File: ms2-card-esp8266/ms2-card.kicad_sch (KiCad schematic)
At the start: 63 parts, among them J1 Schaltregler, J10 MicroSD_SPI_CD, J11 Conn_01x06, J2 ESP Prog, J20 Smartcard Connector, J21 PogoPin, J22 Card Edge, J23 Conn_01x04, J30 USB_B_Micro, J31 Power Select, J32 Conn_01x03, Q1 MMBT3904, Q2 MMBT3904, Q3 MMBT5401, SW1 RESET, U1 ESP-12F, U10 W25Q128JVIM, U2 FM24C64B, U20 BL1551B, U3 BL1551B, U30 CP2102N-A02-GQFN24R, U4 BL1551B, U6 AMS1117-3.3

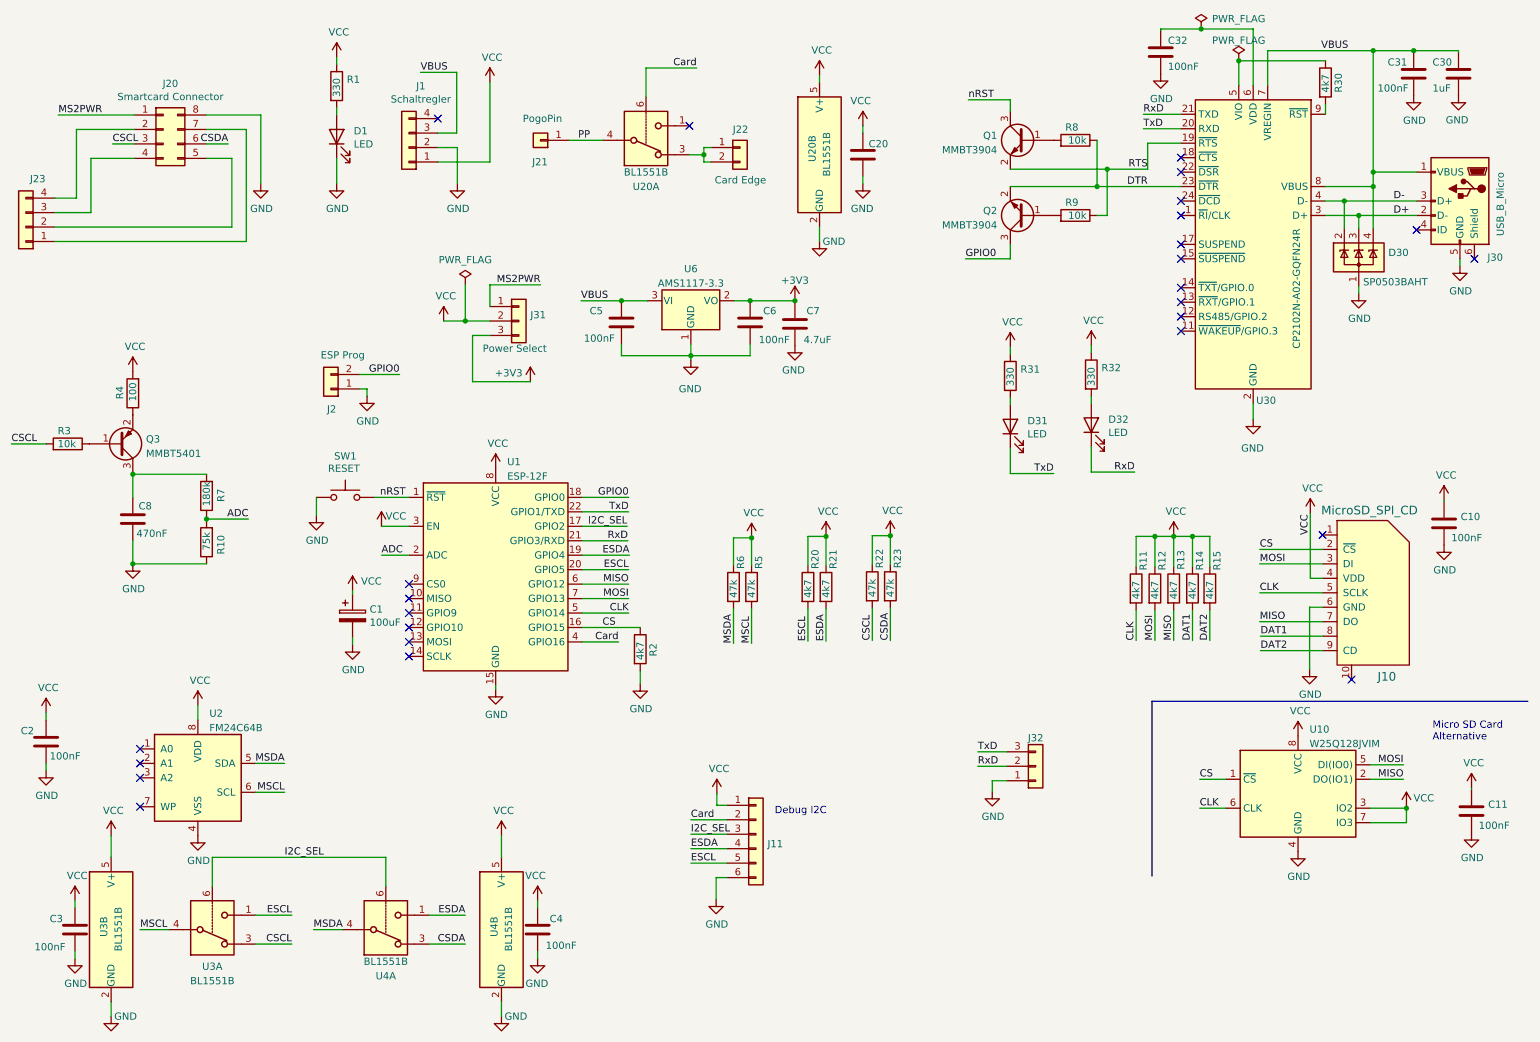
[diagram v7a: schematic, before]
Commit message: switch to KiCad 7 - wip
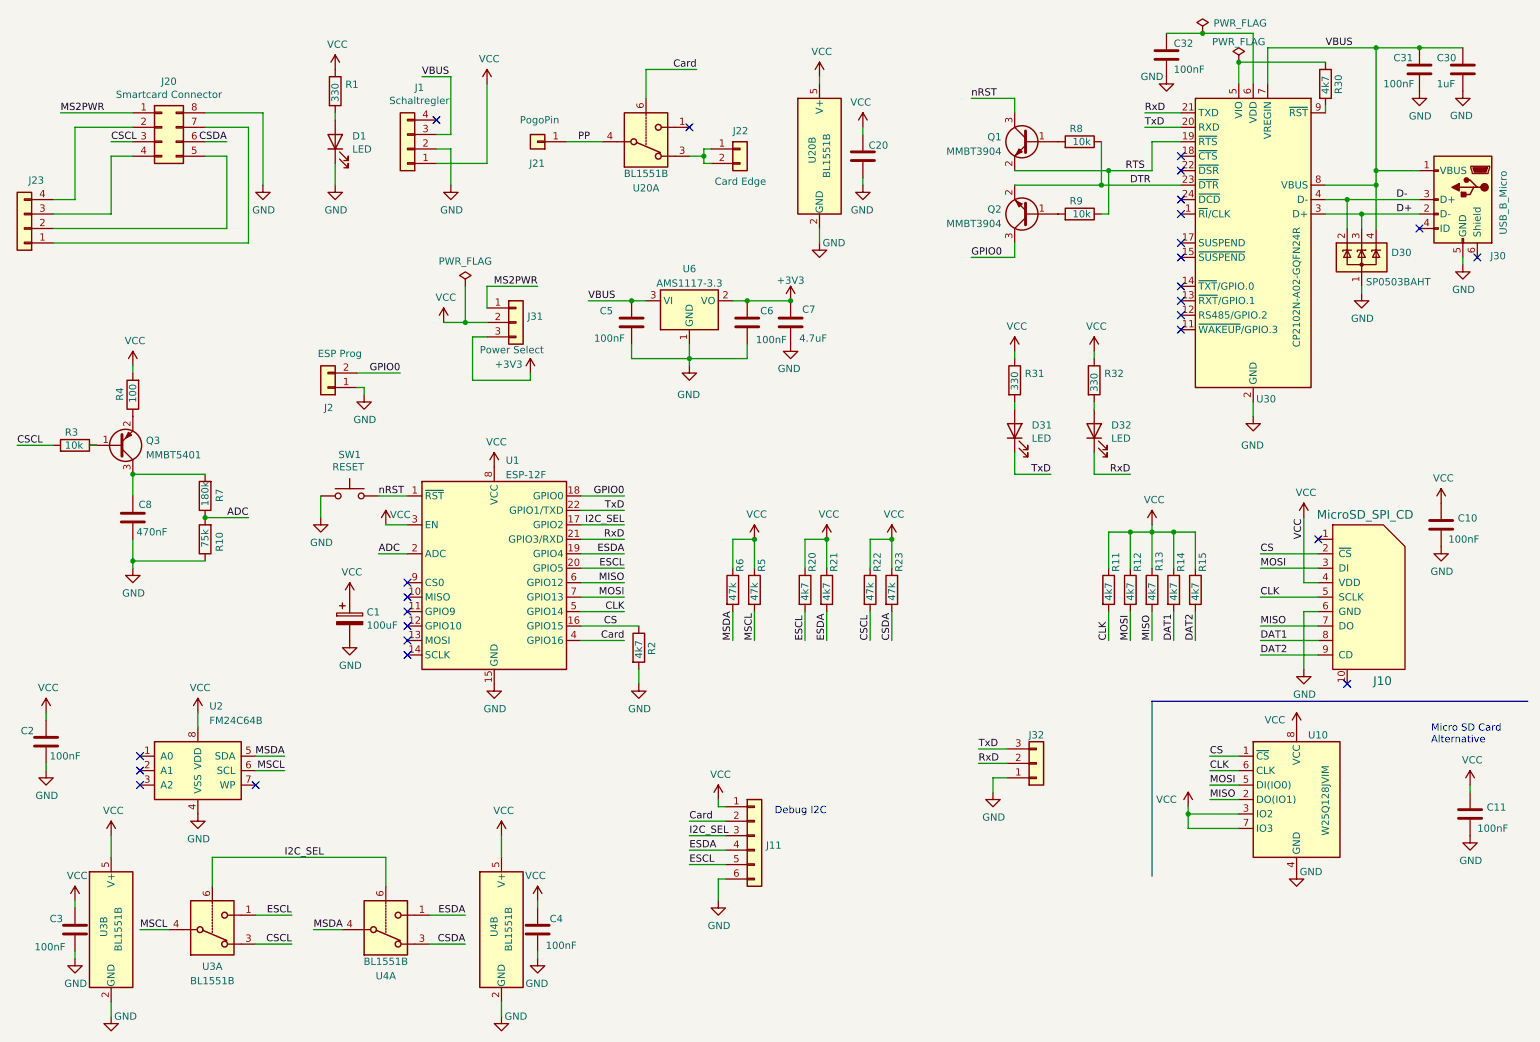
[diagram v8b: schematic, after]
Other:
- moved on the sheet: C1, C10, C11, C30, C31, C32, C5, C6, C7, D1, D30, D31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
